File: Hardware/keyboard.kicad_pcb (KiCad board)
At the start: 2 copper layers, 270 x 100 mm, 60 parts, among them M1 Tab, M10 O, M11 P, M12 Backspace, M13 Esc, M14 A, M15 S, M16 D, M17 F, M18 G, M19 H, M2 Q, M20 J, M21 K, M22 L, M23 ;, M24 ', M25 Shift, M26 Z, M27 X, M28 C, M29 V, M3 W, M30 B, M31 N, M32 M, M33 ,, M34 ., M35 /, M36 Enter, M37 Blnk, M38 Ctrl, M39 Alt, M4 E, M40 Super, M41 Down, M42 Space, M43 Up, M44 L_Ar, M45 D_Ar, M46 U_Ar, M47 R_Ar, M5 R, M6 T, M7 Y, M8 U, M9 I, U1 ROW_1, U2 ROW_2, U3 ROW_3, U4 ROW_4

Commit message: Rerouting.
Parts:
- removed U4: ROW_4, Hardware:SOIC127P1030X265-28N
- C1: value Pi Pico -> SeeeduinoXIAO; footprint Hardware:Seeeduino XIAO-MOUDLE14P-2.54-21X17.8MM -> Hardware:SeeeduinoXIAO-MOUDLE14P-2.54-21X17.8MM
- U1, U2, U3: footprint Hardware:SOIC127P1030X265-28N -> Package_DIP:DIP-28_W7.62mm
- moved C1 232.1 mm to (309.4, 91.4), turned to 270 degrees
- moved U3 102.4 mm to (176.3, 107.7), turned to 90 degrees
- moved U2 61.3 mm to (139.8, 107.7), turned to 90 degrees
- moved U1 20.2 mm to (103.3, 107.7), turned to 90 degrees
- moved R1 16.5 mm to (70.9, 115.3)
- moved R2 16.5 mm to (71.8, 112.4)
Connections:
- C1 pad 4: /INT_0x3 -> (no net)
- U1 pad 1: /ROW_1_3 -> /ROW_1_0
- U1 pad 2: /ROW_1_2 -> /ROW_1_1
- U1 pad 3: /ROW_1_1 -> /ROW_1_2
- U1 pad 4: /ROW_1_0 -> /ROW_1_3
- U1 pad 5: (no net) -> /ROW_2_3
- U1 pad 6: (no net) -> /ROW_2_2
- U1 pad 7: (no net) -> /ROW_2_1
- U1 pad 8: (no net) -> /ROW_2_0
- U2 pad 1: /ROW_2_3 -> /ROW_3_3
- U2 pad 2: /ROW_2_2 -> /ROW_3_2
- U2 pad 3: /ROW_2_1 -> /ROW_3_1
- U2 pad 4: /ROW_2_0 -> /ROW_3_0
- U2 pad 5: (no net) -> /ROW_3_4
- U2 pad 6: (no net) -> /ROW_3_5
- U2 pad 7: (no net) -> /ROW_3_6
- U2 pad 8: (no net) -> /ROW_3_7
- U3 pad 1: /ROW_3_3 -> /ROW_4_2
- U3 pad 2: /ROW_3_2 -> /ROW_4_1
- U3 pad 21: /ROW_3_4 -> /ROW_3_8
- U3 pad 22: /ROW_3_5 -> /ROW_3_9
- U3 pad 23: /ROW_3_6 -> /ROW_3_10
- U3 pad 24: /ROW_3_7 -> /ROW_3_11
- U3 pad 25: /ROW_3_8 -> /ROW_4_3
- U3 pad 26: /ROW_3_9 -> /ROW_4_4
- U3 pad 27: /ROW_3_10 -> /ROW_4_5
- U3 pad 28: /ROW_3_11 -> /ROW_4_6
- U3 pad 3: /ROW_3_1 -> /ROW_4_0
- U3 pad 4: /ROW_3_0 -> /ROW_4_7
- U3 pad 5: (no net) -> /ROW_4_8
- U3 pad 6: (no net) -> /ROW_4_9
- U3 pad 7: (no net) -> /ROW_4_10
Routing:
- net /ROW_3_11: track 237.8 -> 0.00 mm
- net /ROW_1_11: track 237.7 -> 0.00 mm
- net /ROW_2_11: track 237.3 -> 0.00 mm
- net /ROW_4_10: track 237.1 -> 0.00 mm
- net /ROW_1_10: track 218.8 -> 0.00 mm
- net /ROW_2_10: track 218.8 -> 0.00 mm
- net /ROW_3_10: track 218.4 -> 0.00 mm
- net /ROW_4_9: track 218.2 -> 0.00 mm
- net /ROW_2_9: track 200.4 -> 0.00 mm
- net /ROW_1_9: track 199.9 -> 0.00 mm
- net /ROW_3_9: track 199.6 -> 0.00 mm
- net /ROW_4_8: track 199.3 -> 0.00 mm
- net +5V: track 193.0 -> 0.00 mm, vias 8 -> 0
- net /ROW_2_8: track 181.6 -> 0.00 mm
- net /ROW_1_8: track 181.0 -> 0.00 mm
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
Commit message: Moved location of I/O
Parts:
- removed H4: MountingHole, MountingHole:MountingHole_3.2mm_M3_Pad
- M1, M10, M11, M12, M13, M14, M15, M16, M17, M18, M19, M2, M20, M21, M22, M23, M24, M25, M26, M27, M28, M29, M3, M30, M31, M32, M33, M34, M35, M36, M37, M38, M39, M4, M40, M41, M43, M44, M45, M46, M47, M5, M6, M7, M8, M9: footprint Hardware:SW_Kailh_Choc_V1_1.00u -> Hardware:SW_Cherry_MX_1.00u_PCB
- M42: footprint Hardware:SW_Kailh_Choc_V1_2.00u -> Hardware:SW_Cherry_MX_2.00u_PCB
- moved H3 240.6 mm to (311.1, 181.0)
- moved R1 217.9 mm to (287.3, 90.5), turned to 90 degrees
- moved R2 213.3 mm to (284.2, 93.4), turned to 270 degrees
- moved H6 212.7 mm to (120.7, 181.0)
- moved U1 160.5 mm to (263.3, 95.7), turned to 270 degrees
- moved H1 130.6 mm to (215.9, 147.6)
- moved H5 117.0 mm to (282.6, 98.5)
- moved U2 61.6 mm to (200.3, 95.7), turned to 270 degrees
- moved H2 53.5 mm to (149.2, 98.5)
- moved U3 40.8 mm to (137.3, 95.7), turned to 270 degrees
- moved C1 24.7 mm to (292.9, 109.8), turned to 0 degrees
- moved M17 5.32 mm to (189.7, 133.3)
- moved M21 5.32 mm to (265.9, 133.3)
- moved M22 5.32 mm to (285.0, 133.3)
- moved M23 5.32 mm to (304.0, 133.3)
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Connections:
- C1 pad 5: /INT_0x2 -> /INT_0x0
- C1 pad 7: /INT_0x0 -> /INT_0x2
- U1 pad 1: /ROW_1_0 -> /ROW_1_11
- U1 pad 2: /ROW_1_1 -> /ROW_3_11
- U1 pad 21: /ROW_1_4 -> /ROW_4_7
- U1 pad 22: /ROW_1_5 -> /ROW_2_8
- U1 pad 23: /ROW_1_6 -> /ROW_4_8
- U1 pad 24: /ROW_1_7 -> /ROW_2_9
- U1 pad 25: /ROW_1_8 -> /ROW_4_9
- U1 pad 26: /ROW_1_9 -> /ROW_2_10
- U1 pad 27: /ROW_1_10 -> /ROW_4_10
- U1 pad 28: /ROW_1_11 -> /ROW_2_11
- U1 pad 3: /ROW_1_2 -> /ROW_1_10
- U1 pad 4: /ROW_1_3 -> /ROW_3_10
- U1 pad 5: /ROW_2_3 -> /ROW_1_9
- U1 pad 6: /ROW_2_2 -> /ROW_3_9
- U1 pad 7: /ROW_2_1 -> /ROW_1_8
- U1 pad 8: /ROW_2_0 -> /ROW_3_8
- U2 pad 1: /ROW_3_3 -> /ROW_1_7
- U2 pad 2: /ROW_3_2 -> /ROW_3_7
- U2 pad 21: /ROW_2_4 -> /ROW_4_4
- U2 pad 22: /ROW_2_5 -> /ROW_2_4
- U2 pad 23: /ROW_2_6 -> /ROW_4_5
- U2 pad 24: /ROW_2_7 -> /ROW_2_5
- U2 pad 25: /ROW_2_8 -> /ROW_3_6
- U2 pad 26: /ROW_2_9 -> /ROW_1_6
- U2 pad 27: /ROW_2_10 -> /ROW_4_6
- U2 pad 28: /ROW_2_11 -> /ROW_2_7
- U2 pad 3: /ROW_3_1 -> (no net)
- U2 pad 4: /ROW_3_0 -> /ROW_2_6
- U2 pad 5: /ROW_3_4 -> /ROW_1_5
- U2 pad 7: /ROW_3_6 -> /ROW_1_4
- U2 pad 8: /ROW_3_7 -> /ROW_3_4
- U3 pad 1: /ROW_4_2 -> /ROW_1_3
- U3 pad 2: /ROW_4_1 -> /ROW_3_3
- U3 pad 21: /ROW_3_8 -> /ROW_1_0
- U3 pad 22: /ROW_3_9 -> /ROW_3_0
- U3 pad 23: /ROW_3_10 -> /ROW_4_1
- U3 pad 24: /ROW_3_11 -> /ROW_2_1
- U3 pad 25: /ROW_4_3 -> /ROW_4_2
- U3 pad 26: /ROW_4_4 -> /ROW_2_2
- U3 pad 27: /ROW_4_5 -> /ROW_4_3
- U3 pad 28: /ROW_4_6 -> /ROW_2_3
- U3 pad 3: /ROW_4_0 -> /ROW_1_2
- U3 pad 4: /ROW_4_7 -> /ROW_3_2
- U3 pad 5: /ROW_4_8 -> /ROW_1_1
- U3 pad 6: /ROW_4_9 -> /ROW_3_1
- U3 pad 7: /ROW_4_10 -> /ROW_4_0
- U3 pad 8: (no net) -> /ROW_2_0
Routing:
- net +5V: track 0.00 -> 235.2 mm, vias 0 -> 7
- net /SCL_: track 0.00 -> 198.5 mm, vias 0 -> 2
- net /SDA_: track 0.00 -> 194.1 mm, vias 0 -> 2
- net /INT_0x2: track 0.00 -> 178.3 mm, vias 0 -> 1
- net /ROW_4_10: track 0.00 -> 116.8 mm
- net /INT_0x1: track 0.00 -> 115.4 mm, vias 0 -> 1
- net /ROW_3_11: track 0.00 -> 104.8 mm
- net /ROW_1_6: track 142.6 -> 37.9 mm
- net /ROW_4_6: track 0.00 -> 102.9 mm
- net /ROW_4_9: track 0.00 -> 100.8 mm
- net /ROW_1_5: track 122.6 -> 30.5 mm
- net /ROW_3_7: track 0.00 -> 91.4 mm
- net /ROW_3_10: track 0.00 -> 89.4 mm
- net /ROW_4_3: track 0.00 -> 87.8 mm
- net /ROW_4_8: track 0.00 -> 86.3 mm
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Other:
- board size 270 x 100 mm -> 228.6 x 97.6 mm

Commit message: updated output files.
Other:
- board size 228.6 x 97.6 mm -> 228.8 x 97.4 mm

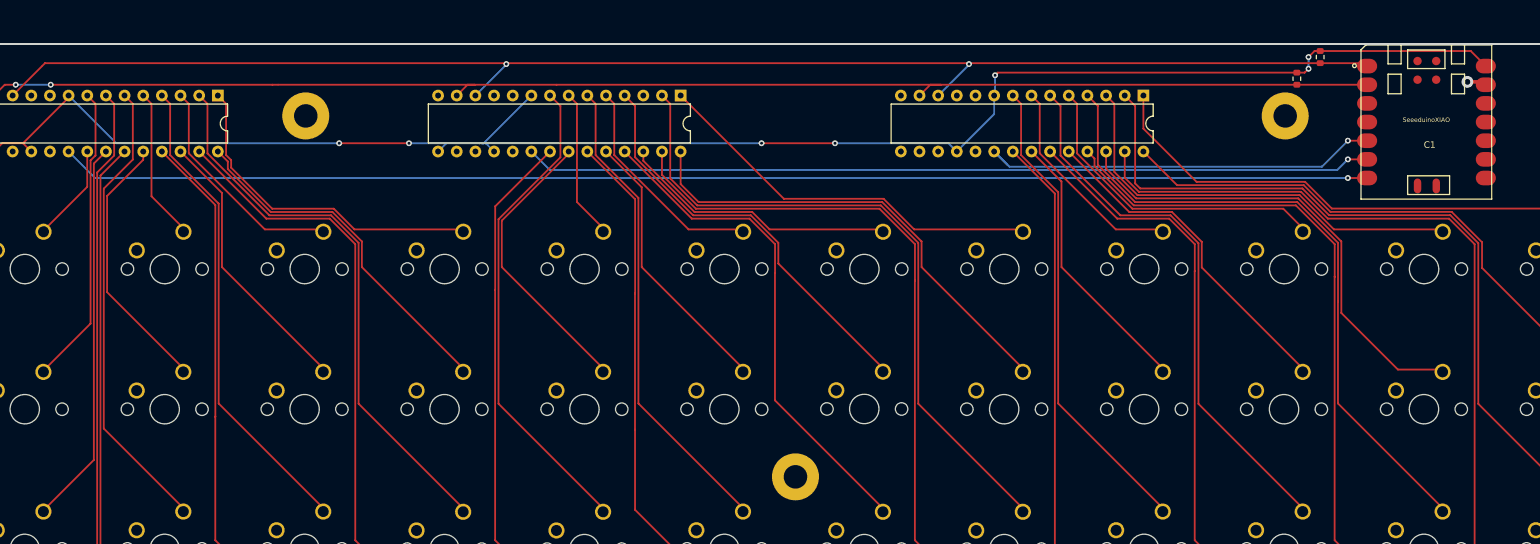
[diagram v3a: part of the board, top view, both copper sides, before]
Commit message: Conversion to all through-hole components.
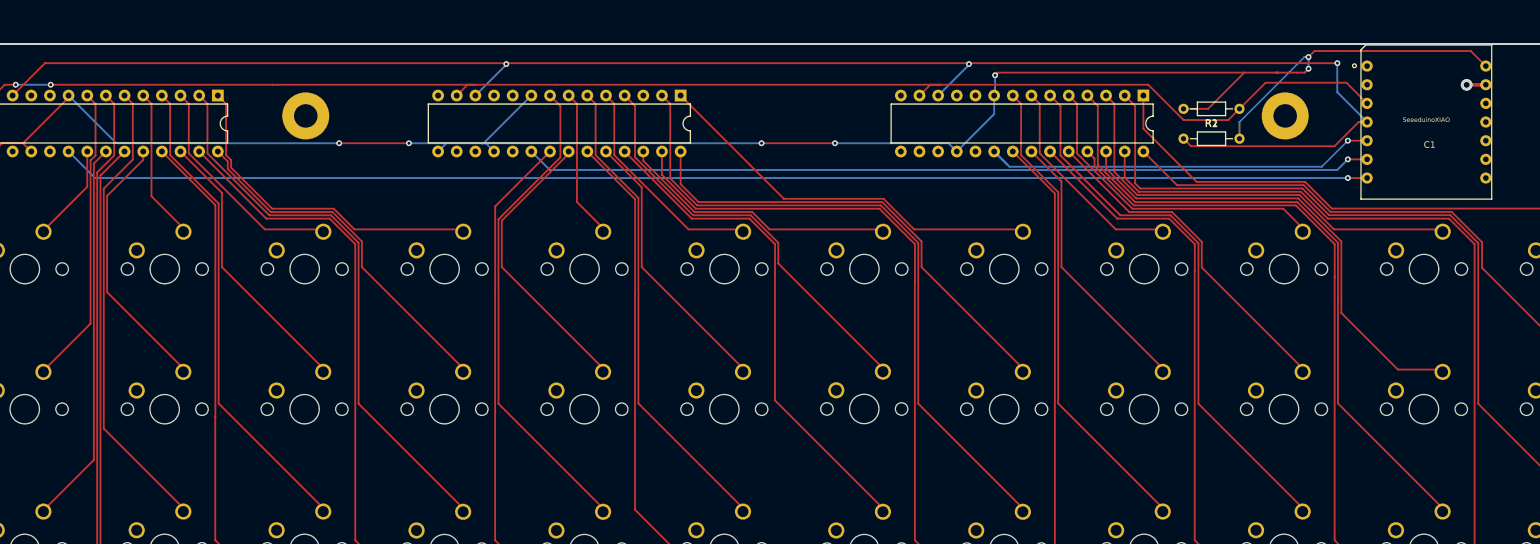
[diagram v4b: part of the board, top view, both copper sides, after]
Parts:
- removed H1: MountingHole, MountingHole:MountingHole_3.2mm_M3_Pad
- R1, R2: footprint Resistor_SMD:R_0603_1608Metric -> Resistor_THT:R_Axial_DIN0204_L3.6mm_D1.6mm_P7.62mm_Horizontal
- moved R1 13.1 mm to (276.4, 97.5), turned to 180 degrees
- moved R2 11.3 mm to (276.4, 101.6), turned to 180 degrees
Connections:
- C1 pad 1: /SCL_ -> (no net)
- C1 pad 2: /SDA_ -> (no net)
- C1 pad 3: (no net) -> /SDA_
- C1 pad 4: (no net) -> /SCL_
- R1 pad 1: /SCL_ -> /SDA_
- R2 pad 2: /SDA_ -> /SCL_
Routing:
- net /SCL_: track 198.5 -> 230.7 mm, vias 2 -> 3
- net +5V: track 235.2 -> 261.2 mm
- net /SDA_: track 194.1 -> 199.4 mm
- net (no net): track 0.00 -> 0.56 mm
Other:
- board text added: ""Write bussy on it" -Suyash"
- board text removed: "Created, with love, by Helmut Lord"
